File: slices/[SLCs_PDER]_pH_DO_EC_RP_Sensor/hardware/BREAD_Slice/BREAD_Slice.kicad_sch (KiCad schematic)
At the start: 16 parts, among them J1 I2C_01x04, J2 Conn_01x10_Female

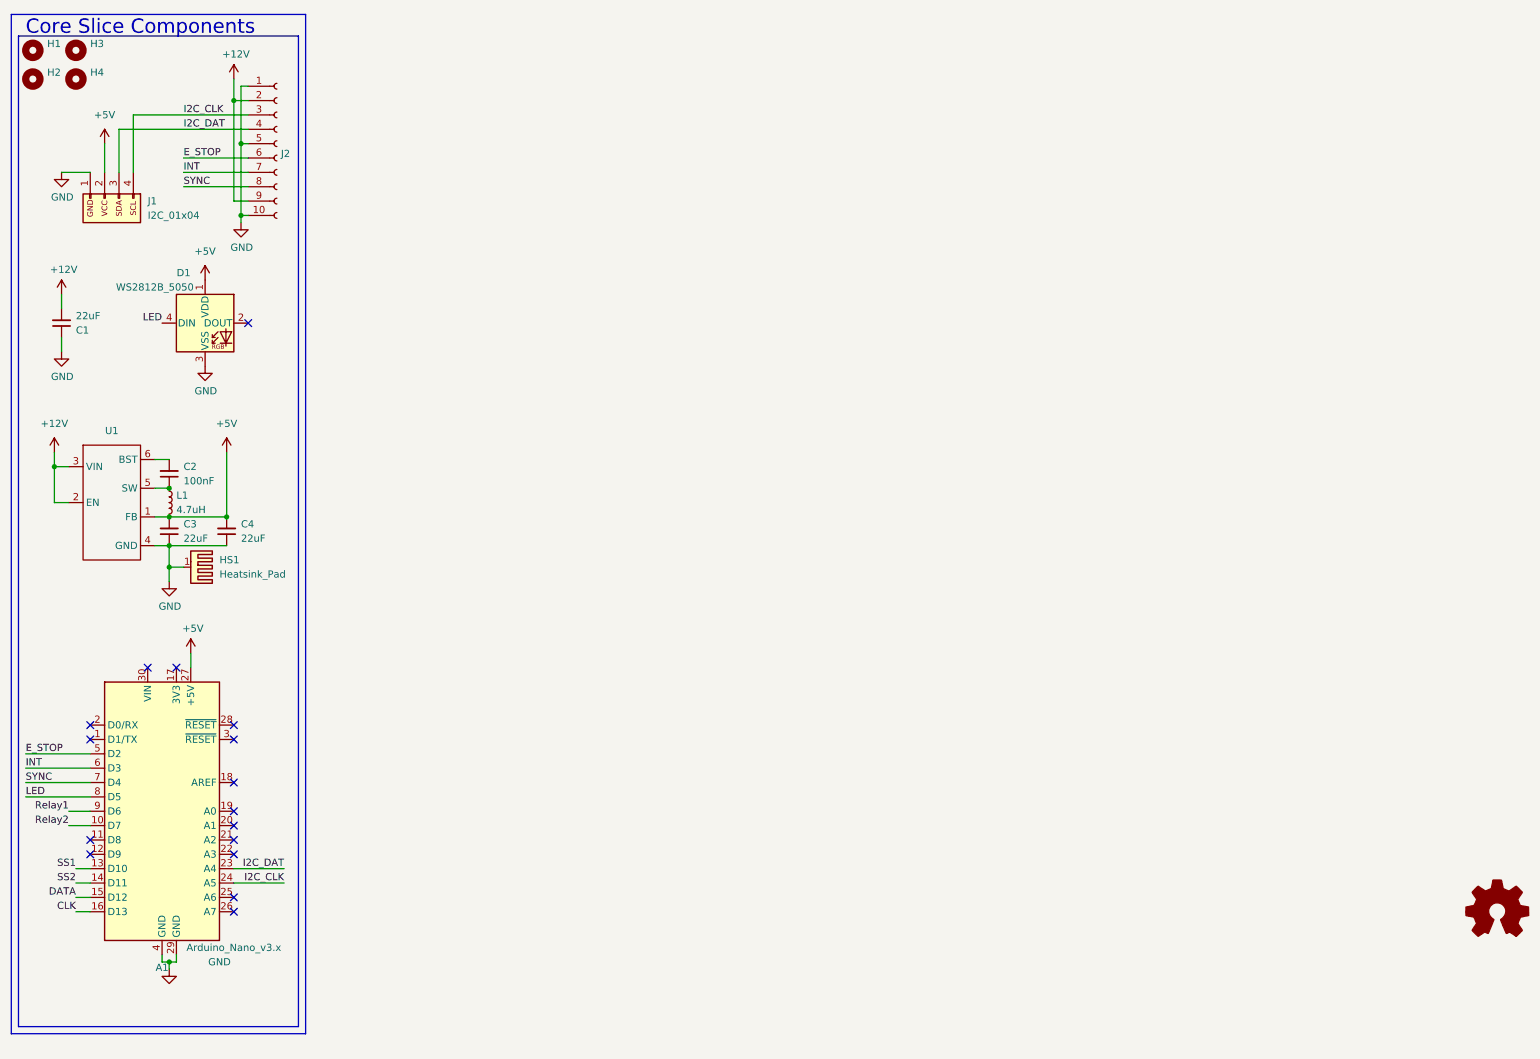
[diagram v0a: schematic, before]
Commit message: improved phdo and initial ERC pass on PDER
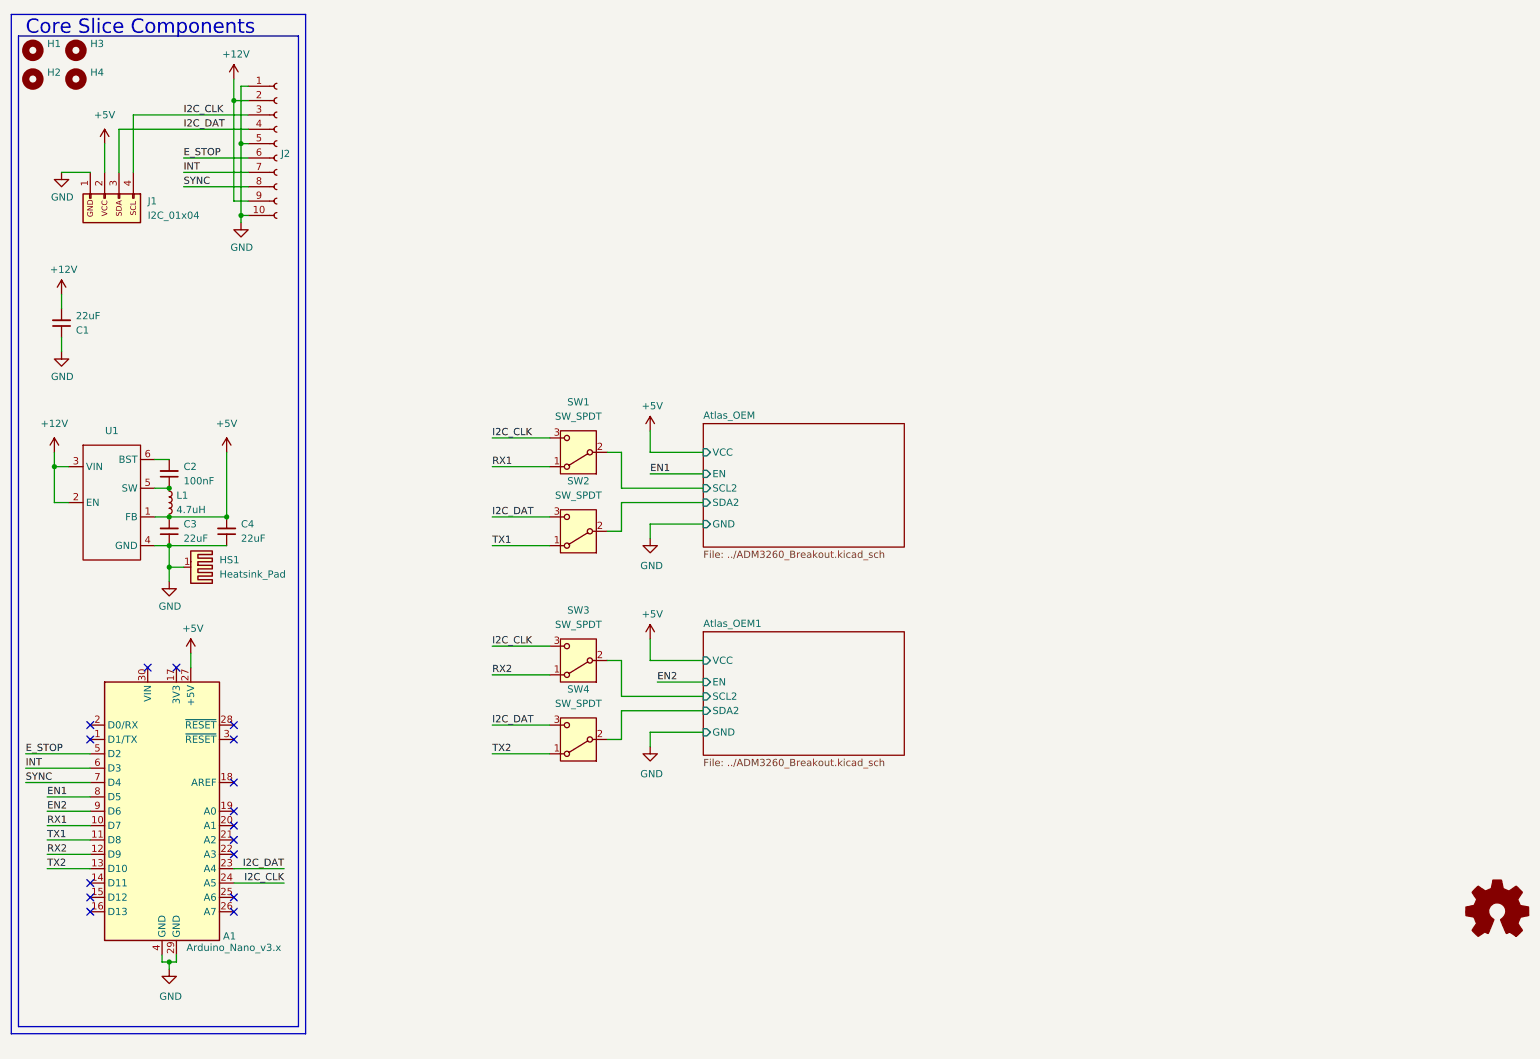
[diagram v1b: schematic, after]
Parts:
- removed D1: WS2812B_5050, SparkFun-LED:WS2812-5050-4PIN, symbol SparkFun-LED:WS2812B_5050
- added SW1, SW2: SW_SPDT, Capacitor_SMD:C_0201_0603Metric, symbol Switch:SW_SPDT
- added SW3: SW_SPDT, Package_TO_SOT_SMD:SOT-23-3, symbol Switch:SW_SPDT
- added SW4: SW_SPDT, Connector_Coaxial:BNC_Amphenol_B6252HB-NPP3G-50_Horizontal, symbol Switch:SW_SPDT
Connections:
- net I2C_CLK: now also SW1.3 (C), SW3.3 (C)
- net I2C_DAT: now also SW2.3 (C), SW4.3 (C)
- net TX1: now reaches A1.11 (D8)
- net TX1: now also SW2.1 (A)
- net RX2: now reaches A1.12 (D9)
- net RX2: now also SW3.1 (A)
- net CLK: no longer names the net of A1.16 (D13)
- net DATA: no longer names the net of A1.15 (D12)
- net LED renamed EN1
- net Relay1 renamed EN2
- net Relay2 renamed RX1
- net RX1: now also SW1.1 (A)
- net SS1 renamed TX2
- net TX2: now also SW4.1 (A)
- net SS2: no longer names the net of A1.14 (D11)
- new net Atlas_OEM/SCL2: SW1.2 (B)
- new net Atlas_OEM/SDA2: SW2.2 (B)
- new net Atlas_OEM1/SCL2: SW3.2 (B)
- new net Atlas_OEM1/SDA2: SW4.2 (B)
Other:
- added sheet Atlas_OEM (../ADM3260_Breakout.kicad_sch)
- added sheet Atlas_OEM1 (../ADM3260_Breakout.kicad_sch)

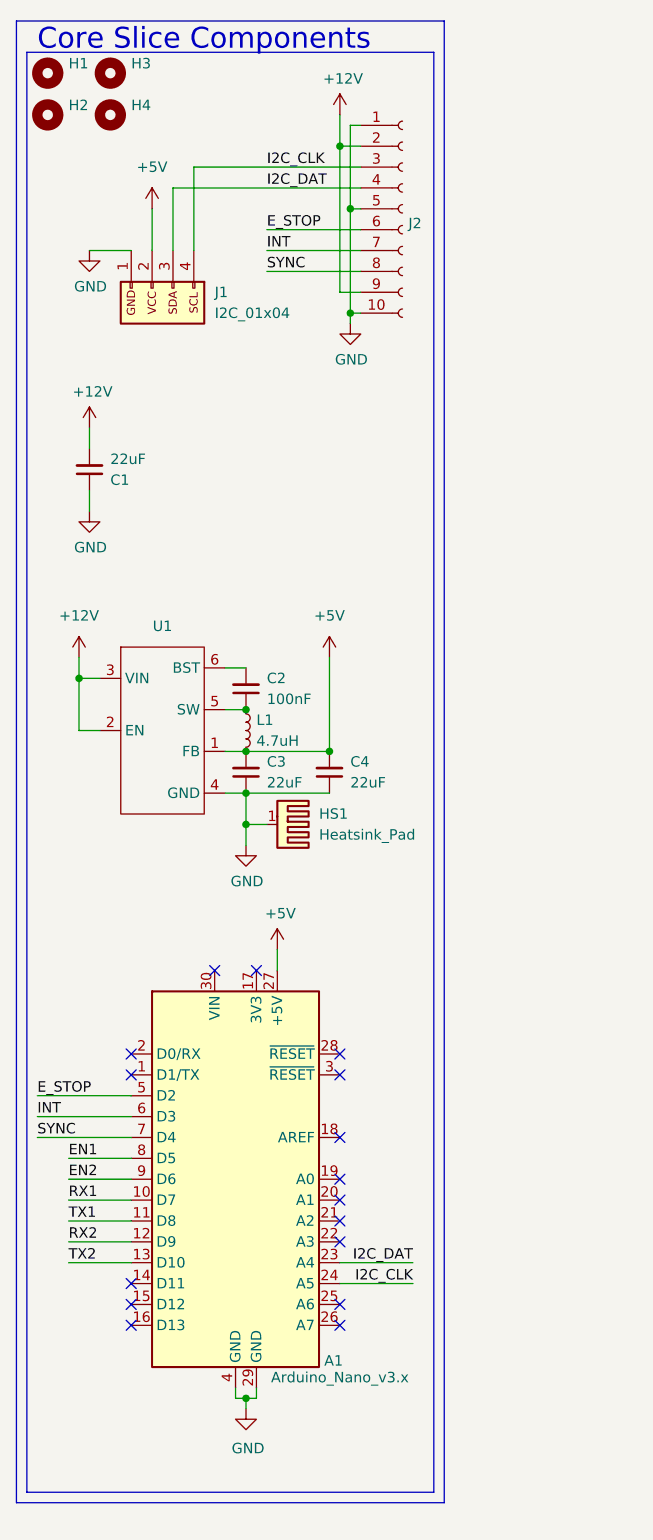
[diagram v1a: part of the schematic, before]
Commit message: atlas oem slice footprints all done and at routing stage
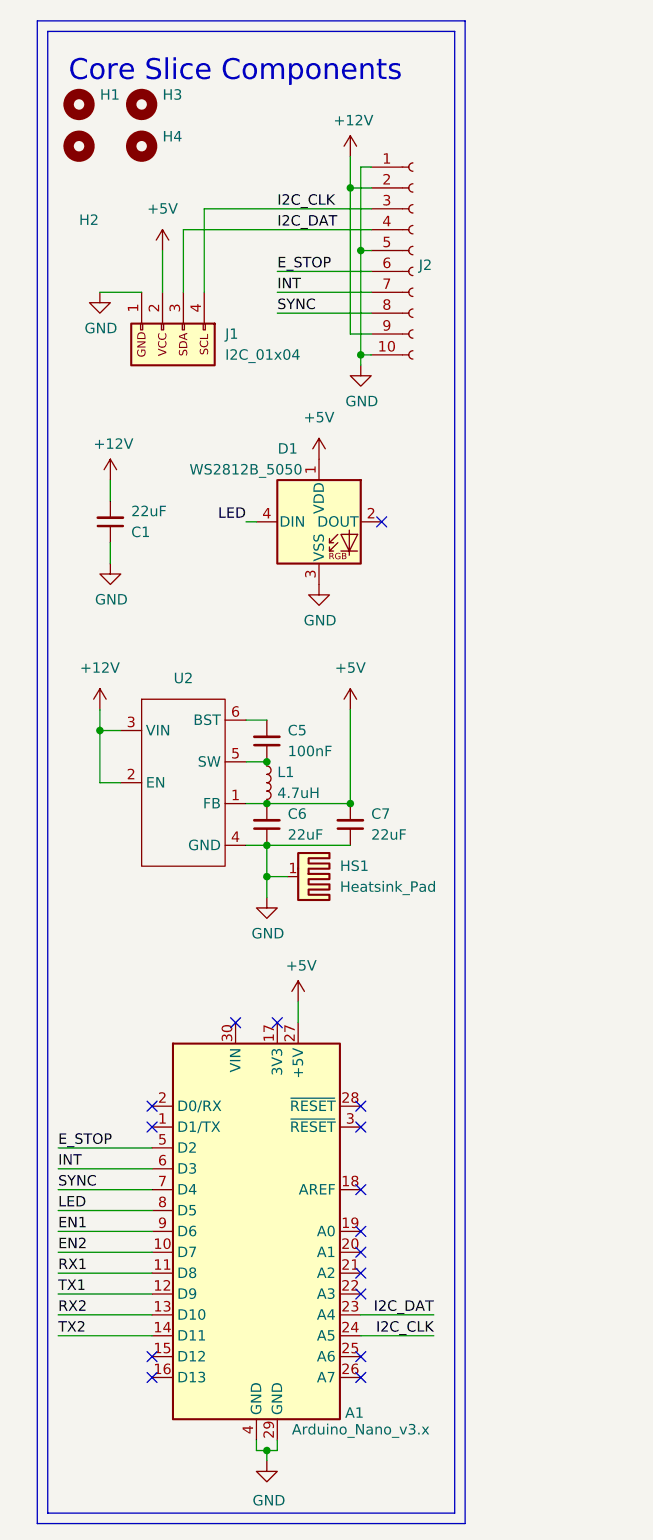
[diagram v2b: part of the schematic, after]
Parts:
- removed C2: 100nF, Capacitor_SMD:C_1206_3216Metric, symbol Device:C_Small
- removed C3, C4: 22uF, Capacitor_SMD:C_1206_3216Metric, symbol Device:C_Small
- removed U1: ~, Package_TO_SOT_SMD:TSOT-23-6, symbol SparkFun-DiscreteSemi:AP63205
- added C5: 100nF, Capacitor_SMD:C_1206_3216Metric, symbol Device:C_Small
- added C6, C7: 22uF, Capacitor_SMD:C_1206_3216Metric, symbol Device:C_Small
- added D1: WS2812B_5050, SparkFun-LED:WS2812-5050-4PIN, symbol SparkFun-LED:WS2812B_5050
- added U2: ~, Package_TO_SOT_SMD:TSOT-23-6, symbol SparkFun-DiscreteSemi:AP63205
- HS1: footprint SparkFun-Fuse:Thermal Pad -> KML-Custom:Thermal Pad
- SW1, SW2: footprint Capacitor_SMD:C_0201_0603Metric -> SparkFun-Switch:Slide_SPDT_PTH_11.6x4.0mm
- SW3: footprint Package_TO_SOT_SMD:SOT-23-3 -> SparkFun-Switch:Slide_SPDT_PTH_11.6x4.0mm
- SW4: footprint Connector_Coaxial:BNC_Amphenol_B6252HB-NPP3G-50_Horizontal -> SparkFun-Switch:Slide_SPDT_PTH_11.6x4.0mm
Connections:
- net +12V: now also U2.2 (EN), U2.3 (VIN)
- net +5V: now also C6.2, C7.2, D1.1 (VDD), U2.1 (FB)
- net EN1: now also A1.9 (D6); no longer A1.8 (D5)
- net EN2: now also A1.10 (D7); no longer A1.9 (D6)
- net GND: now also C6.1, C7.1, D1.3 (VSS), U2.4 (GND)
- net RX1: now also A1.11 (D8); no longer A1.10 (D7)
- net RX2: now also A1.13 (D10); no longer A1.12 (D9)
- net TX1: now also A1.12 (D9); no longer A1.11 (D8)
- net TX2: now also A1.14 (D11); no longer A1.13 (D10)
- net at L1.1: now also C5.1, U2.5 (SW)
- new net: C5.2, U2.6 (BST)
- new net LED: A1.8 (D5), D1.4 (DIN)
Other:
- moved on the sheet: A1, H1, H2, H3, H4, J1, J2
